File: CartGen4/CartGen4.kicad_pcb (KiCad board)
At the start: 4 copper layers, 52.8 x 60.9 mm, 77 parts, among them J1 MEM2080-00-128-00-A, SW1 SW_Push, U1 TPS65266-1RHBR, U10 IS25WP080D-JNLE, U11 DS1391U-33+, U2 SN74LV1T34DCKR, U3 SIT8008BI-73-33E-33.333333G, U4 NXS0108BQX, U5 AS1C8M16PL-70BIN, U6 NXS0108BQX, U7 NXS0108BQX, U8 NXS0104BQX, U9 LFXP2-8E-5MN132C, Y1 FC-135R 32.7680KA-E5

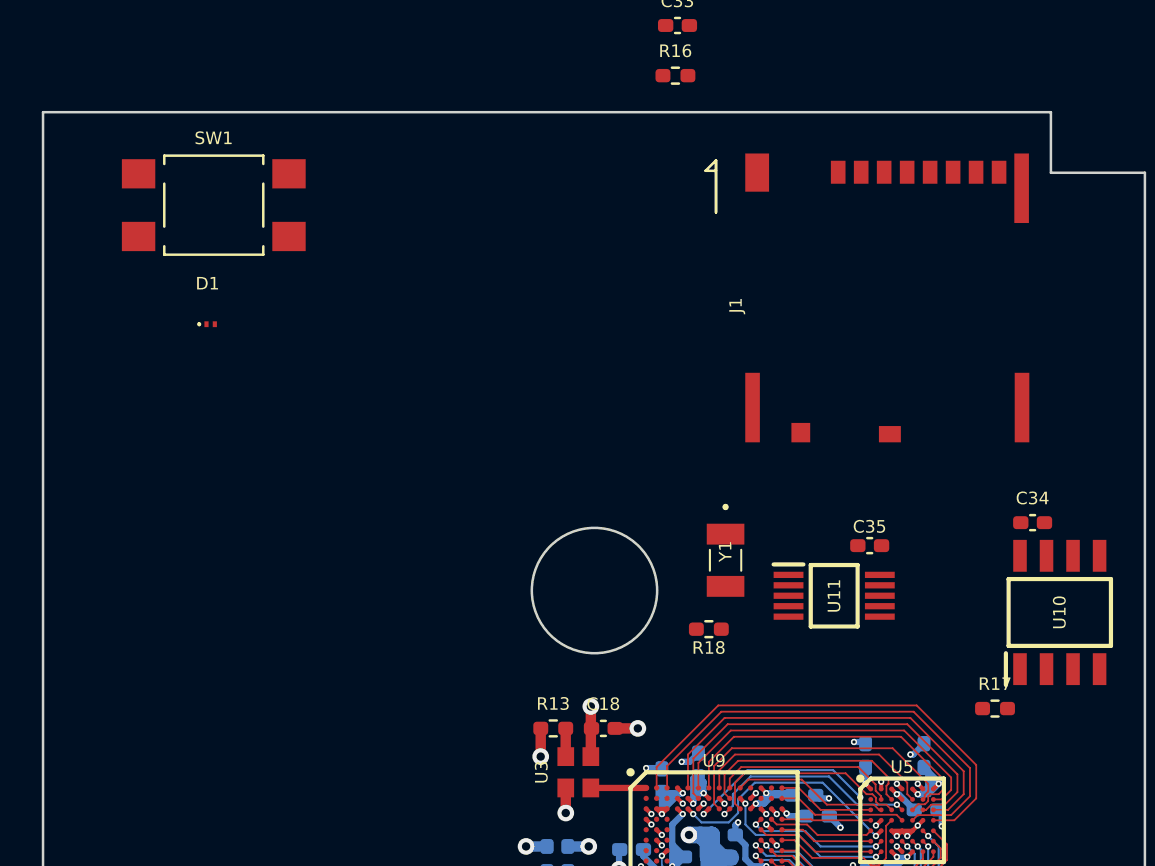
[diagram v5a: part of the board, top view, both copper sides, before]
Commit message: Chose battery retainer
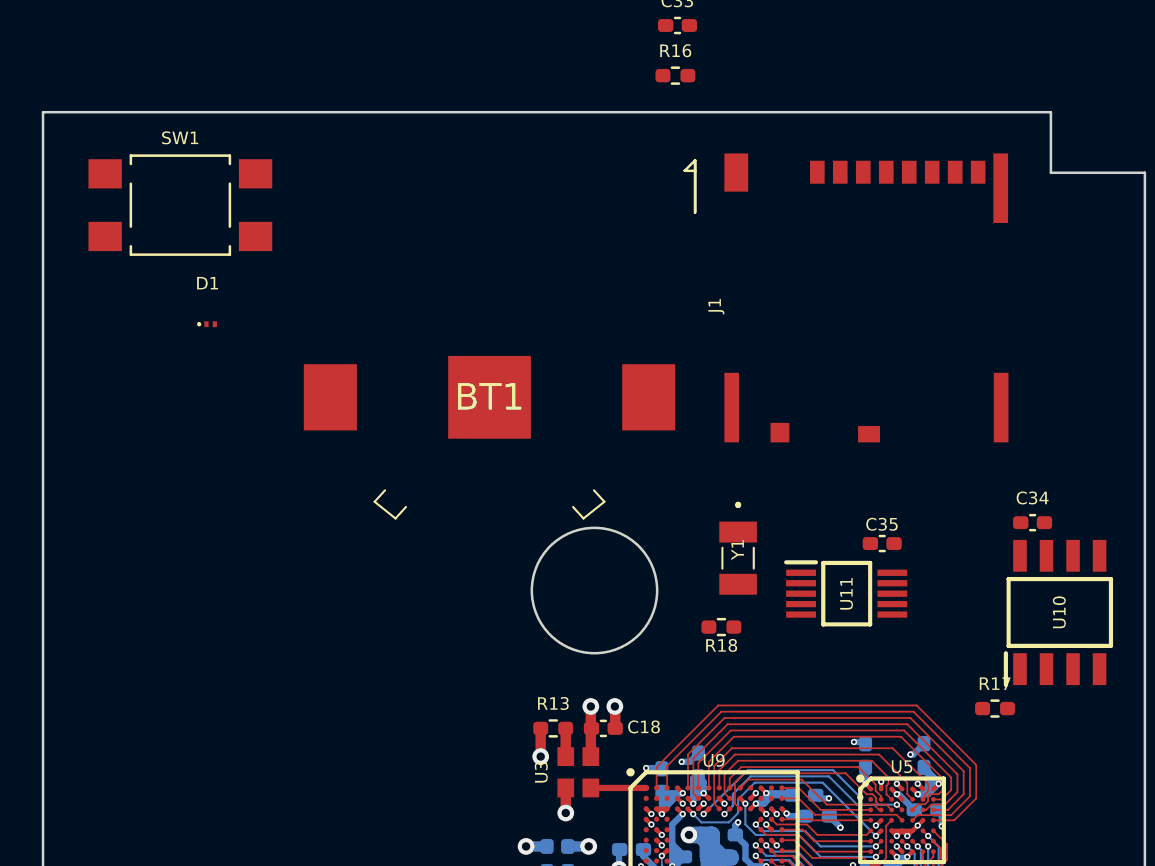
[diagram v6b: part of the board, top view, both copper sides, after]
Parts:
- BT1: footprint Battery:Battery_CR1225 -> SamacSys_Parts:2894
- moved SW1 1.60 mm to (46.2, 42.5)
- moved BT1 1.57 mm to (61.0, 51.7), turned to 180 degrees
- moved J1 1.00 mm to (76.3, 40.4)
- moved Y1 0.61 mm to (72.9, 59.4)
- moved U11 0.61 mm to (78.1, 61.1)
- moved C35 0.61 mm to (79.8, 58.7)
- moved R18 0.61 mm to (72.1, 62.7)
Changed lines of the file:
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@@
   (net 157 "Net-(BT1-Pad1)")
   (footprint "SamacSys_Parts:MEM2080-00-128-00-A" (layer "F.Cu")
-    (at 77.3425 40.375)
+    (at 76.3425 40.375)
     (property "Critical" "Y")
     (property "Description" "Memory Card Connectors Micro SD, Push Push, SMT, Card Entry Normal, 1.28 mm profile")
@@
       (polygon
         (pts
-          (xy 85.9825 52.925)
-          (xy 81.9825 52.925)
-          (xy 81.9825 50.525)
-          (xy 76.9825 50.525)
-          (xy 76.9825 45.075)
-          (xy 85.9825 45.075)
+          (xy 84.9825 52.925)
+          (xy 80.9825 52.925)
+          (xy 80.9825 50.525)
+          (xy 75.9825 50.525)
+          (xy 75.9825 45.075)
+          (xy 84.9825 45.075)
         )
       )
@@
   )
   (footprint "Button_Switch_SMD:SW_SPST_TL3305A" (layer "F.Cu")
-    (at 47.8 42.5)
+    (at 46.2 42.5)
     (descr "https://www.e-switch.com/system/asset/product_line/data_sheet/213/TL3305.pdf")
     (tags "TL3305 Series Tact Switch")
@@
   )
   (footprint "SamacSys_Parts:SOP50P490X110-10N" (layer "F.Cu")
-    (at 77.5 61.2)
+    (at 78.1 61.1)
     (descr "10L UMAX/USOP")
     (tags "Integrated Circuit")
@@
   )
   (footprint "Resistor_SMD:R_0402_1005Metric_Pad0.72x0.64mm_HandSolder" (layer "F.Cu")
-    (at 71.5 62.8)
+    (at 72.1 62.7)
     (descr "Resistor SMD 0402 (1005 Metric), square (rectangular) end terminal, IPC_7351 nominal with elongated pad for handsoldering. (Body size source: IPC-SM-782 page 72, https://www.pcb-3d.com/wordpress/wp-content/uploads/ipc-sm-782a_amendment_1_and_2.pdf), generated with kicad-footprint-generator")
     (tags "resistor handsolder")
@@
     (property "Source" "ANY")
     (attr smd)
-    (fp_text reference "C18" (at 0 -1.16) (layer "F.SilkS")
+    (fp_text reference "C18" (at 1.95 -0.05) (layer "F.SilkS")
       (effects (font (size 0.6 0.6) (thickness 0.125)))
     )
@@
     )
   )
-  (footprint "Battery:Battery_CR1225" (layer "F.Cu")
-    (at 62.4 51)
-    (descr "CR1225 battery")
-    (tags "battery CR1225 coin cell")
+  (footprint "SamacSys_Parts:2894" (layer "F.Cu")
+    (at 61 51.7 180)
+    (descr "2894-3")
+    (tags "Hardware")
     (property "Critical" "N")
     (property "Notes" "Battery is utilised and maintained by the DS1391U-33+ RTC.")
@@
     (property "Sheetname" "spi")
     (property "Source" "SPEC")
-    (attr exclude_from_pos_files)
-    (fp_text reference "BT1" (at 0 -1) (layer "F.SilkS") hide
-      (effects (font (size 0.6 0.6) (thickness 0.125)))
+    (attr smd)
+    (fp_text reference "BT1" (at 0 0) (layer "F.SilkS")
+      (effects (font (size 1.27 1.27) (thickness 0.254)))
     )
-    (fp_text value "Battery_Cell" (at 0 0.5) (layer "F.Fab")
-      (effects (font (size 1 1) (thickness 0.15)))
+    (fp_text value "Battery_Cell" (at 0 0) (layer "F.SilkS") hide
+      (effects (font (size 1.27 1.27) (thickness 0.254)))
     )
-    (fp_circle (center 0 0) (end 6.25 0) (layer "F.Fab") (width 0.1) (fill none))
-    (model "${KICAD6_3DMODEL_DIR}/Battery.3dshapes/Battery_CR1225.wrl"
-      (offset (xyz 0 0 0))
+    (fp_text user "${REFERENCE}" (at 0 0) (layer "F.Fab")
+      (effects (font (size 1.27 1.27) (thickness 0.254)))
+    )
+    (fp_line (start 4.5 -5.8) (end 5.5 -5) (layer "F.SilkS") (width 0.1))
+    (fp_line (start 5.5 -5) (end 5 -4.45) (layer "F.SilkS") (width 0.1))
+    (fp_line (start -4.5 -5.8) (end -4 -5.25) (layer "F.SilkS") (width 0.1))
+    (fp_line (start 4 -5.25) (end 4.5 -5.8) (layer "F.SilkS") (width 0.1))
+    (fp_line (start -5 -4.45) (end -5.5 -5) (layer "F.SilkS") (width 0.1))
+    (fp_line (start -5.5 -5) (end -4.5 -5.8) (layer "F.SilkS") (width 0.1))
+    (fp_line (start -9.89 -7.605) (end 9.89 -7.605) (layer "F.CrtYd") (width 0.1))
+    (fp_line (start 9.89 7.605) (end -9.89 7.605) (layer "F.CrtYd") (width 0.1))
+    (fp_line (start 9.89 -7.605) (end 9.89 7.605) (layer "F.CrtYd") (width 0.1))
+    (fp_line (start -9.89 7.605) (end -9.89 -7.605) (layer "F.CrtYd") (width 0.1))
+    (fp_line (start 6.605 0) (end 6.605 0) (layer "F.Fab") (width 0.2))
+    (fp_line (start 4.5 -5.8) (end 4 -5.25) (layer "F.Fab") (width 0.2))
+    (fp_line (start -5 -4.45) (end -5.5 -5) (layer "F.Fab") (width 0.2))
+    (fp_line (start -4.5 -5.8) (end -4 -5.25) (layer "F.Fab") (width 0.2))
+    (fp_line (start -6.605 0) (end -6.605 0) (layer "F.Fab") (width 0.2))
+    (fp_line (start 5 -4.45) (end 5.5 -5) (layer "F.Fab") (width 0.2))
+    (fp_line (start -5.5 -5) (end -4.5 -5.8) (layer "F.Fab") (width 0.2))
+    (fp_line (start 5.5 -5) (end 4.5 -5.8) (layer "F.Fab") (width 0.2))
+    (fp_arc (start 6.605 0) (mid 0 6.605) (end -6.605 0) (layer "F.Fab") (width 0.2))
+    (fp_arc (start -6.605 0) (mid 0 -6.605) (end 6.605 0) (layer "F.Fab") (width 0.2))
+    (pad "1" smd rect (at -7.62 0 180) (size 2.54 3.17) (layers "F.Cu" "F.Paste" "F.Mask")
+      (net 157 "Net-(BT1-Pad1)") (pinfunction "+") (pintype "passive"))
+    (pad "1" smd rect (at 7.62 0 180) (size 2.54 3.17) (layers "F.Cu" "F.Paste" "F.Mask")
+      (net 157 "Net-(BT1-Pad1)") (pinfunction "+") (pintype "passive"))
+    (pad "2" smd rect (at 0 0 180) (size 3.96 3.96) (layers "F.Cu" "F.Paste" "F.Mask")
+      (net 24 "GND") (pinfunction "-") (pintype "passive"))
+    (model "${KICAD6_3DMODEL_DIR}/Battery.3dshapes/2894.stp"
+      (offset (xyz 0 0 2.42000004))
       (scale (xyz 1 1 1))
-      (rotate (xyz 0 0 0))
+      (rotate (xyz -90 0 0))
     )
   )
@@
   )
   (footprint "SamacSys_Parts:FC135R327680KAE3" (layer "F.Cu")
-    (at 72.3 59.5 -90)
+    (at 72.9 59.4 -90)
     (descr "FC-135R 32.7680KA-E3-5")
     (tags "Crystal or Oscillator")
@@
   )
   (footprint "Capacitor_SMD:C_0402_1005Metric_Pad0.74x0.62mm_HandSolder" (layer "F.Cu")
-    (at 79.2 58.8 180)
+    (at 79.8 58.7 180)
     (descr "Capacitor SMD 0402 (1005 Metric), square (rectangular) end terminal, IPC_7351 nominal with elongated pad for handsoldering. (Body size source: IPC-SM-782 page 76, https://www.pcb-3d.com/wordpress/wp-content/uploads/ipc-sm-782a_amendment_1_and_2.pdf), generated with kicad-footprint-generator")
     (tags "capacitor handsolder")
@@
   (segment (start 47.75 82.05) (end 47 82.8) (width 0.3) (layer "F.Cu") (net 24))
   (segment (start 81.75 71.95) (end 81.25 72.45) (width 0.2) (layer "F.Cu") (net 24))
-  (segment (start 68.1 67.55) (end 67.0175 67.55) (width 0.5) (layer "F.Cu") (net 24))
   (segment (start 51.75 74.9) (end 51.75 77.6) (width 1) (layer "F.Cu") (net 24))
   (segment (start 52.6375 76.15) (end 50.8625 76.15) (width 1) (layer "F.Cu") (net 24))
@@
   (segment (start 58.05 78.4) (end 58.05 81.2875) (width 1) (layer "F.Cu") (net 24))
   (segment (start 46.25 85.25) (end 46.25 83.55) (width 0.3) (layer "F.Cu") (net 24))
+  (segment (start 67 66.5) (end 67.0175 66.5175) (width 0.5) (layer "F.Cu") (net 24))
   (segment (start 70 70.9) (end 70.25 71.15) (width 0.2) (layer "F.Cu") (net 24))
   (segment (start 59 85.55) (end 59.3 85.85) (width 0.3) (layer "F.Cu") (net 24))
@@
   (segment (start 74.5 71.4) (end 74.75 71.65) (width 0.2) (layer "F.Cu") (net 24))
   (segment (start 73 76.4) (end 73.5 75.9) (width 0.2) (layer "F.Cu") (net 24))
+  (segment (start 67.0175 66.5175) (end 67.0175 67.55) (width 0.5) (layer "F.Cu") (net 24))
   (segment (start 80.25 72.45) (end 81.25 72.45) (width 0.2) (layer "F.Cu") (net 24))
   (segment (start 45.75 85.25) (end 45.75 84.05) (width 0.3) (layer "F.Cu") (net 24))
@@
   (via (at 80.5 73.2) (size 0.3024) (drill 0.15) (layers "F.Cu" "B.Cu") (net 24))
   (via (at 69.25 72.65) (size 0.3024) (drill 0.15) (layers "F.Cu" "B.Cu") (net 24))
-  (via (at 68.1 67.55) (size 0.8) (drill 0.4) (layers "F.Cu" "B.Cu") (free) (net 24))
+  (via (at 67 66.5) (size 0.8) (drill 0.4) (layers "F.Cu" "B.Cu") (free) (net 24))
   (via (at 80.5 70.2) (size 0.3024) (drill 0.15) (layers "F.Cu" "B.Cu") (net 24))
   (via (at 73.65 79.7) (size 0.3024) (drill 0.15) (layers "F.Cu" "B.Cu") (net 24))

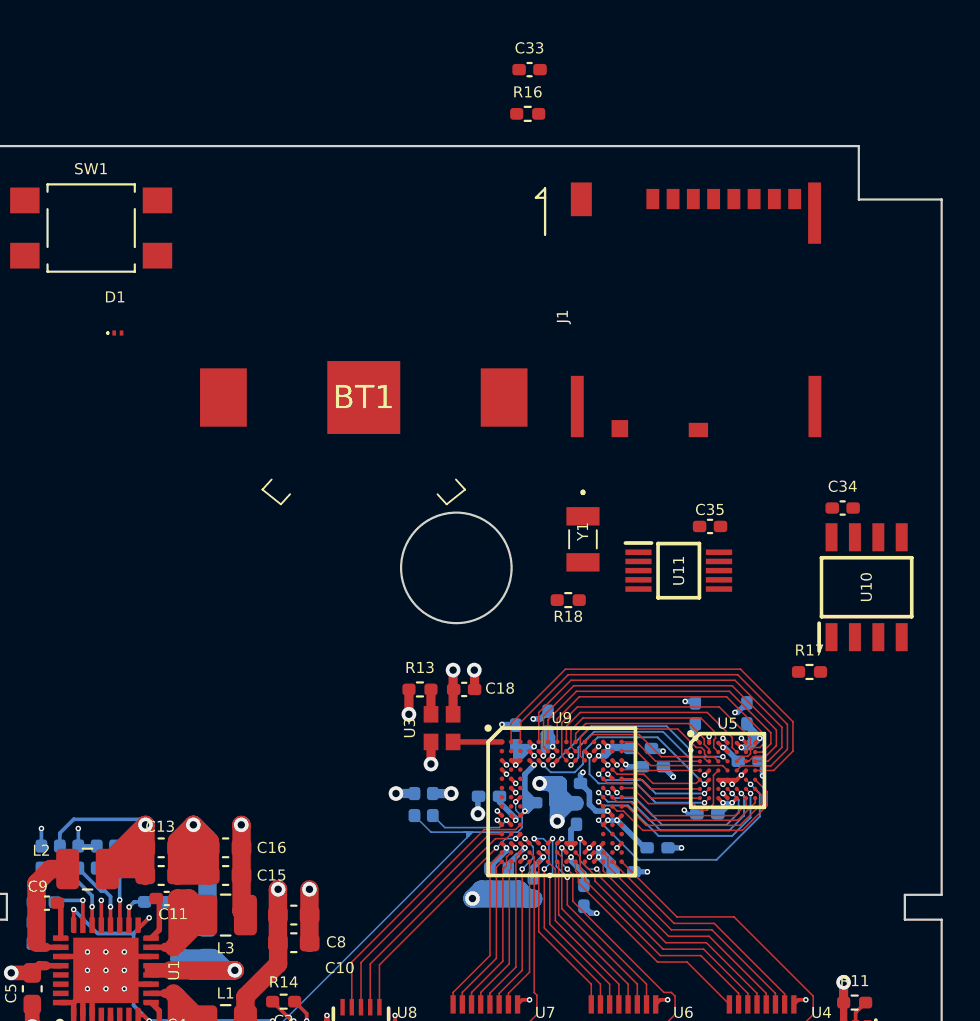
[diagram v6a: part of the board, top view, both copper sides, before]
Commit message: Wired SD power
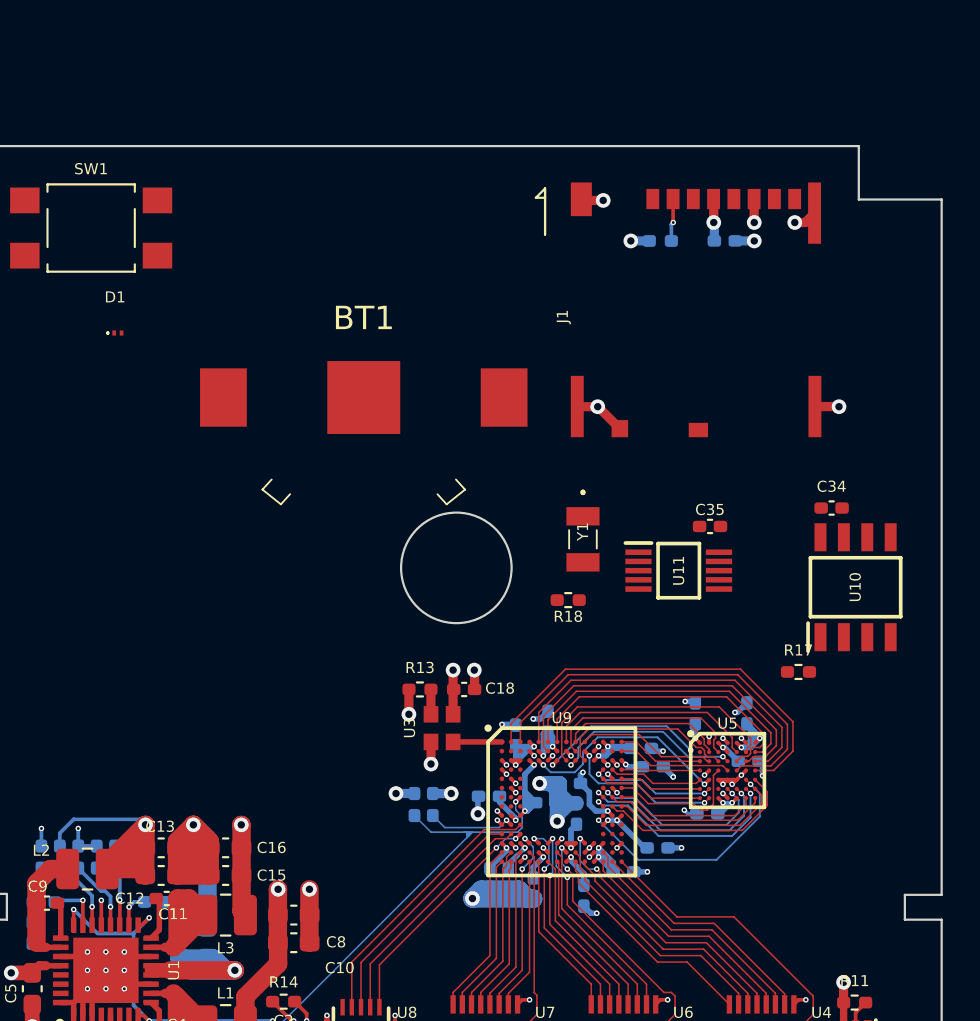
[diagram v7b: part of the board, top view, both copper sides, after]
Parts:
- C33, R16: moved to B.Cu
- moved C33 14.1 mm to (80.6, 43.2)
- moved R16 9.97 mm to (77.1, 43.2)
- moved R17 0.60 mm to (84.6, 66.6)
- moved C34 0.60 mm to (86.4, 57.7)
- moved U10 0.60 mm to (87.7, 62.0)
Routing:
- net GND: track 108.2 -> 117.1 mm, vias 65 -> 71
- net +3V3: track 36.8 -> 40.1 mm, vias 20 -> 22
- net FPGA_SPI_SD_CS#: track 0.00 -> 2.32 mm, vias 0 -> 1

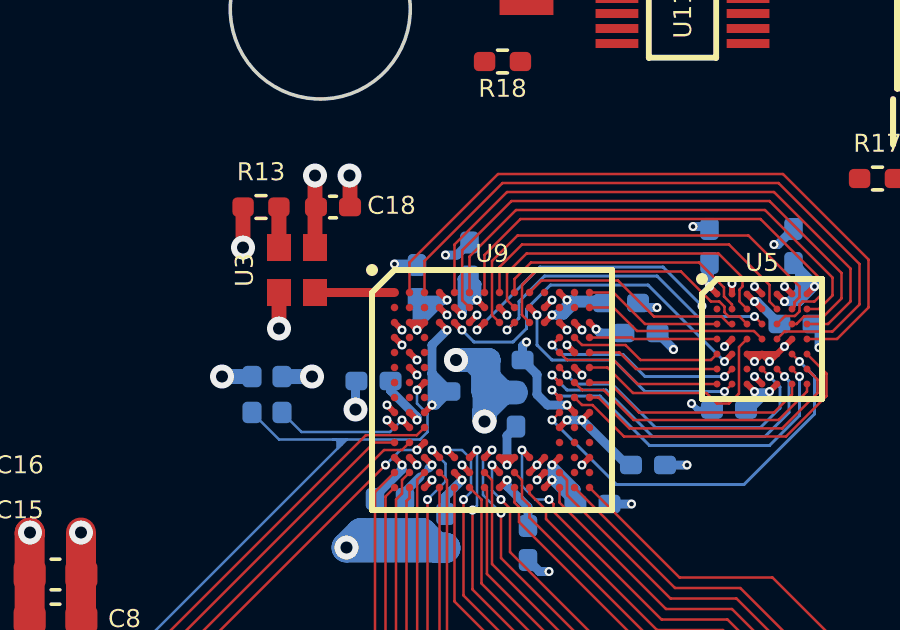
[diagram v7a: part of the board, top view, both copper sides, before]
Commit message: Fanned out SPI bus
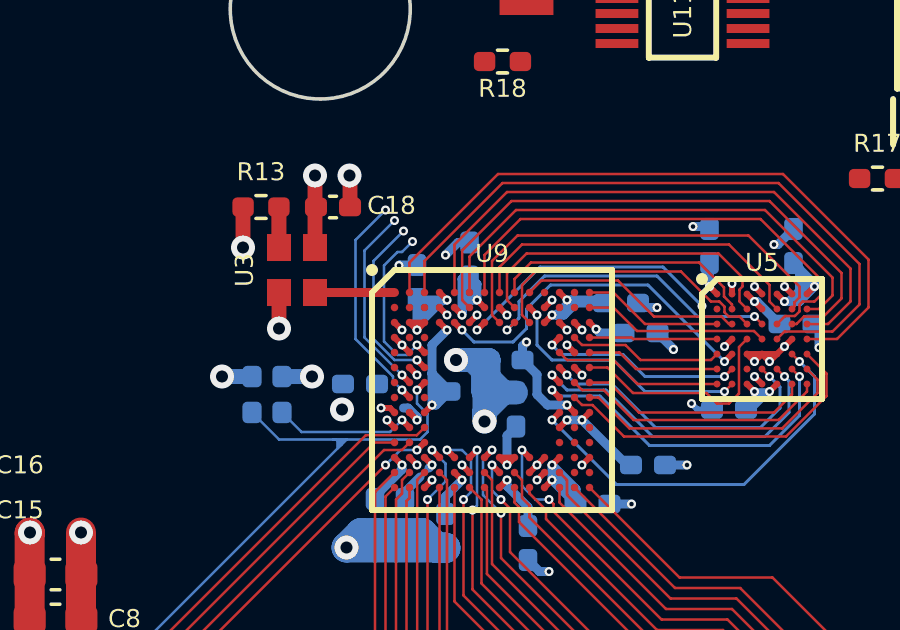
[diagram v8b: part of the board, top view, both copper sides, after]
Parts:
- moved C19 0.46 mm to (67.3, 73.5)
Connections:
- J1 pad DSW2: (no net) -> SD_CARD_DETECT
- U9 pad B1: unconnected-(U9-PadB1) -> FPGA_SPI_RTC_CS#
- U9 pad B2: unconnected-(U9-PadB2) -> FPGA_SPI_SD_CS#
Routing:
- net FPGA_SPI_MOSI: track 0.00 -> 7.41 mm, vias 0 -> 2
- net FPGA_SPI_MISO: track 0.00 -> 6.44 mm, vias 0 -> 2
- net FPGA_SPI_CLK: track 0.00 -> 6.11 mm, vias 0 -> 2
- net FPGA_SPI_FLASH_CS#: track 0.00 -> 5.59 mm, vias 0 -> 2
- net +3V3: track 40.1 -> 39.1 mm
- net GND: track 117.1 -> 116.1 mm, vias 71 -> 70
